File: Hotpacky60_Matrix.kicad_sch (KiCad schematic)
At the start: 127 parts

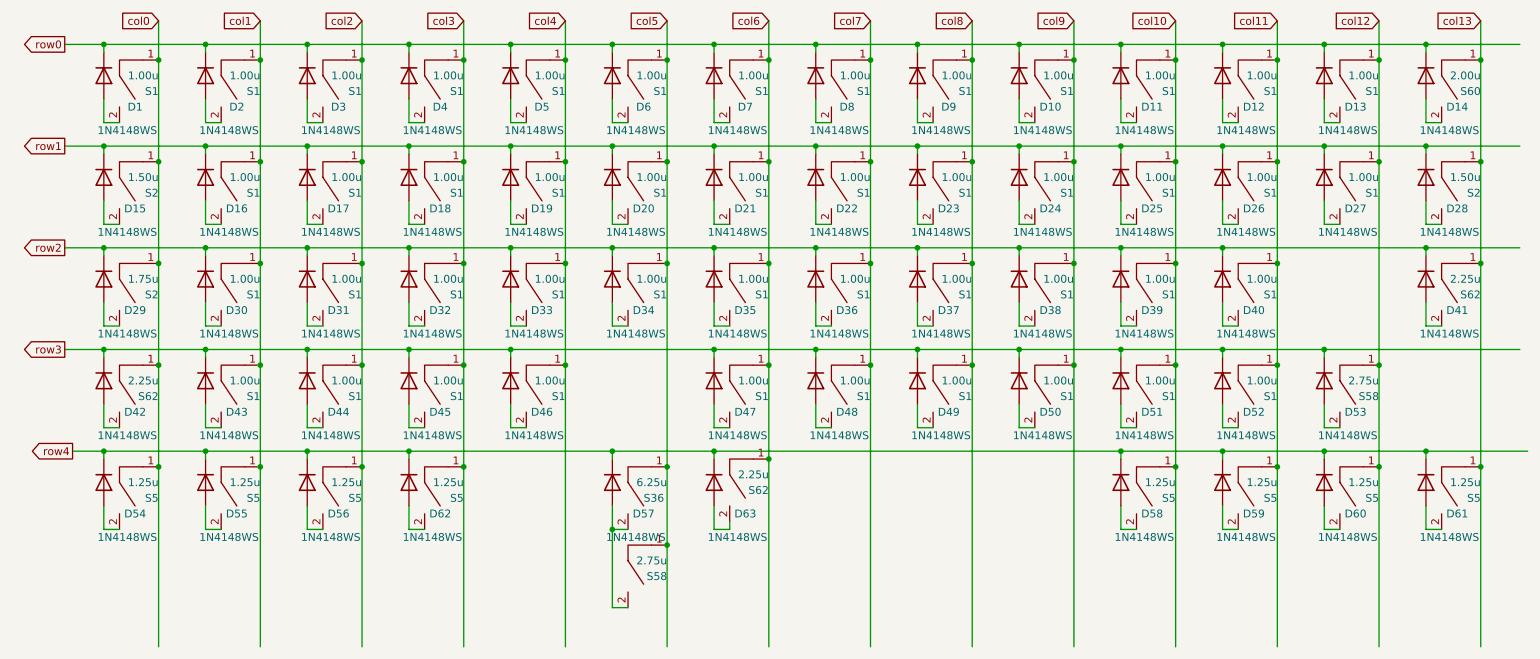
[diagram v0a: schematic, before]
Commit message: replace parts and change pin assignment.
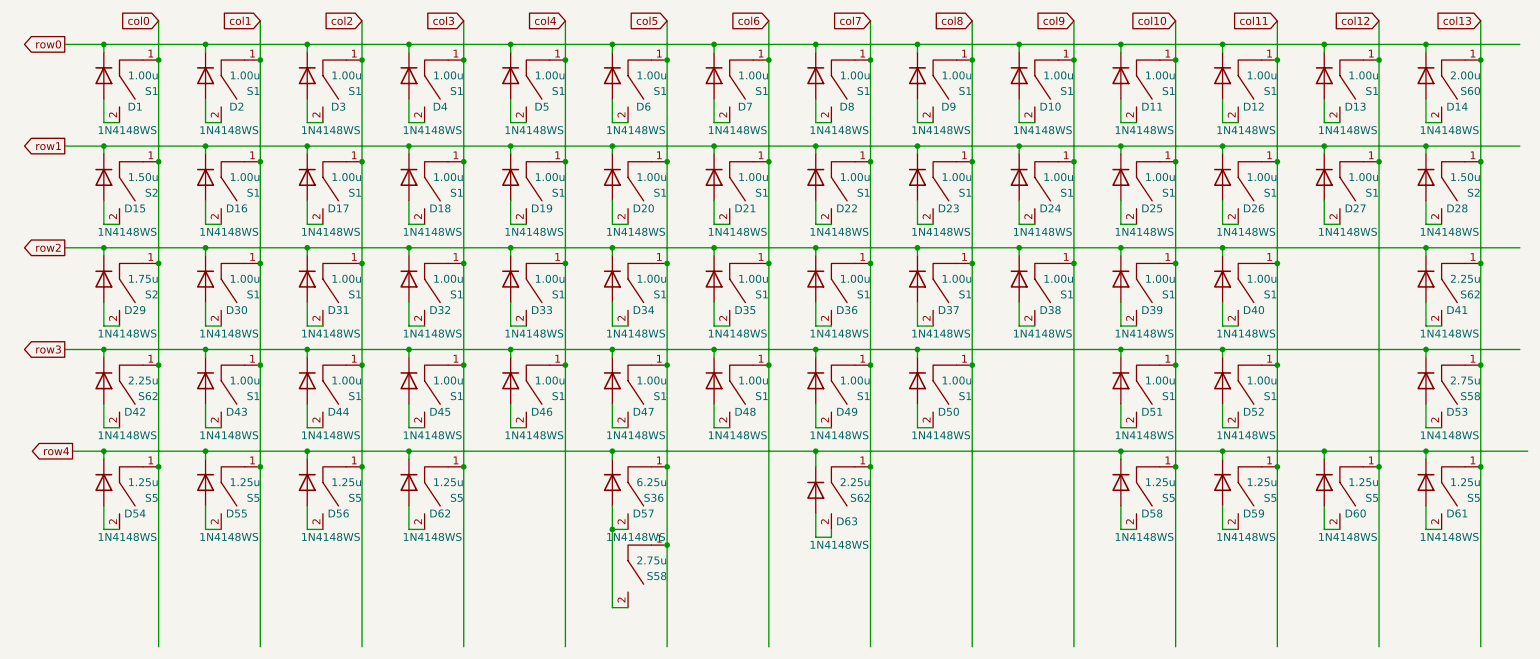
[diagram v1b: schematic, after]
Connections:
- net col12: no longer S58.1
- net col13: now also S58.1
- net col5: now also S1.1
- net col6: now also S1.1; no longer S1.1, S62.1
- net col7: now also S1.1, S62.1; no longer S1.1
- net col8: now also S1.1; no longer S1.1
- net col9: no longer S1.1
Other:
- moved on the sheet: D47, D48, D49, D50, D53, D63, S1, S58, S62

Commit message: Update
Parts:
- removed S1 (x8): 1.00u, Switch_Keyboard_Cherry_MX:SW_Cherry_MX_PCB_1.00u, symbol mx1a-simple:MX1A
- added S1 (x8): 1.00u, Switch_Keyboard_Cherry_MX:SW_Cherry_MX_PCB_1.00u, symbol mx1a-simple:MX1A
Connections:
- net col2: now also S1.1
- net col3: now also S1.1
- net col4: now also S1.1
- net col5: now also S1.1; no longer S36.1, S58.1
- net col6: now also S36.1, S58.1, S1.1
- net col7: now also S1.1; no longer S62.1
- net col8: now also S62.1, S1.1
- net col9: now also S1.1
- net at D49.2 (A): now also S1.2
- net at D46.2 (A): now also S1.2
- net at D45.2 (A): now also S1.2
- net at D44.2 (A): now also S1.2
- net at D50.2 (A): now also S1.2
- net at D48.2 (A): now also S1.2
- net at D43.2 (A): now also S1.2
- net at D47.2 (A): now also S1.2
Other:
- moved on the sheet: D57, D63, S36, S58, S62
